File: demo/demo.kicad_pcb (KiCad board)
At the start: 2 copper layers, 85.7 x 85.7 mm, 31 parts

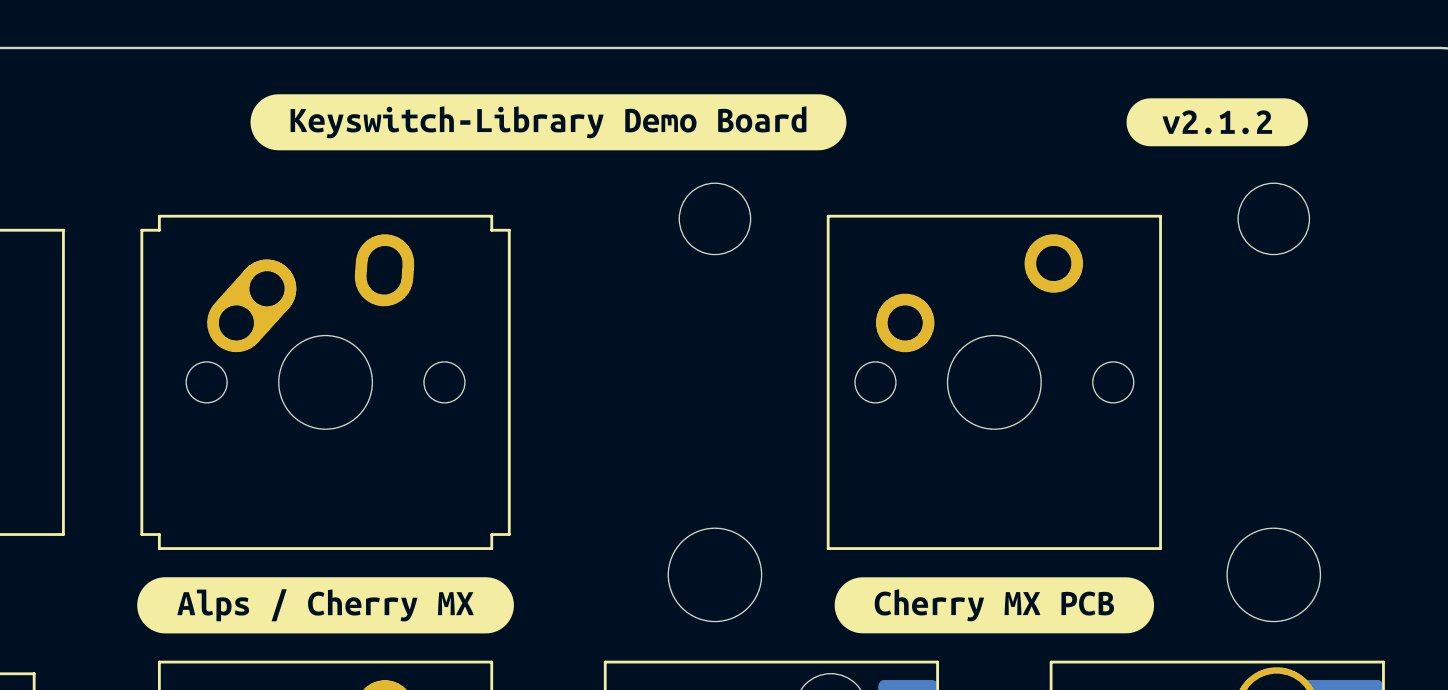
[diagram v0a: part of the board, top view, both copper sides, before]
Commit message: update demo board footprints
Signed-off-by: Rafael Silva <perigoso@riseup.net>
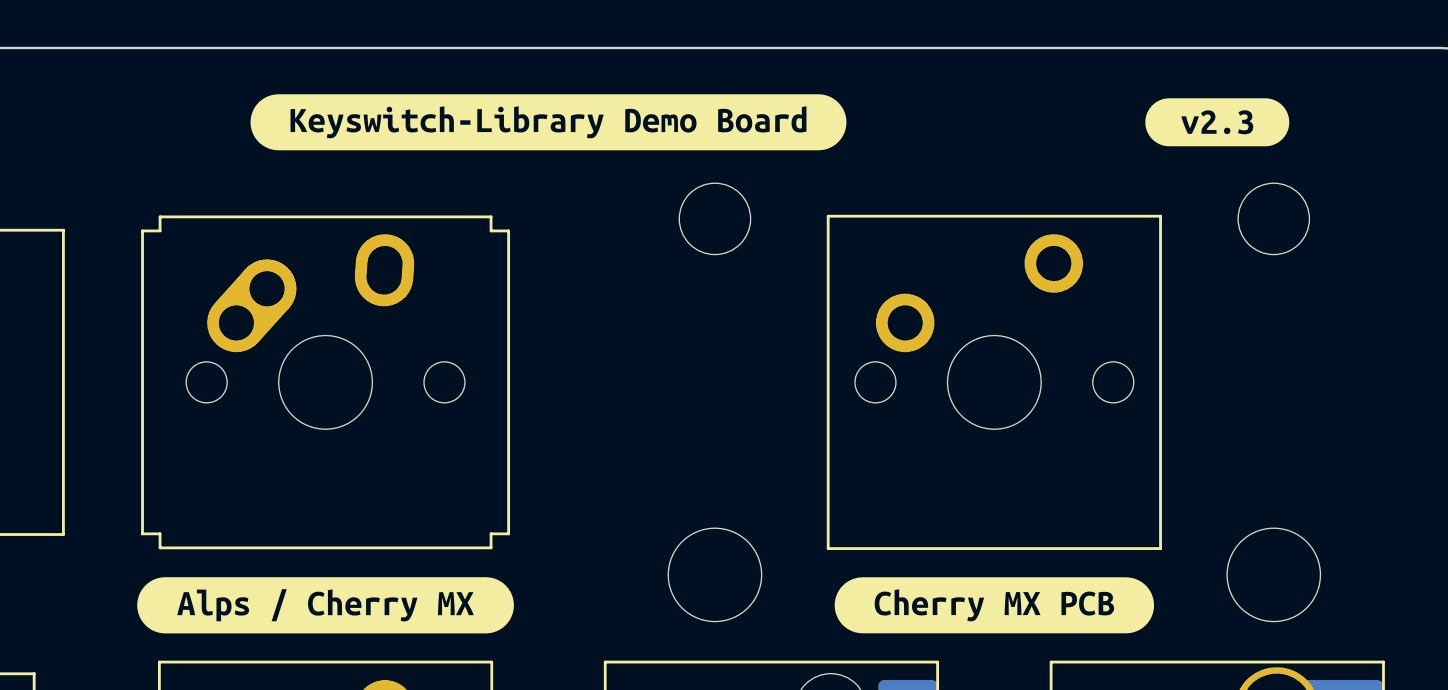
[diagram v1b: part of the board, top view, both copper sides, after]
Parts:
- removed kibuzzard-6232B20F: G***, kibuzzard-6232B20F
- added kibuzzard-629185FF: G***, kibuzzard-629185FF, F.Cu at (114.3, 46.0)
